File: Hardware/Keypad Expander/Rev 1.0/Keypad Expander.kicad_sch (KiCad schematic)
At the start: 11 parts, among them J1 6502 Card Edge, J2 PORT B, J3 PORT A, U1 65C21, U2 AT28C64, U3 74HC138, U4 74HC138

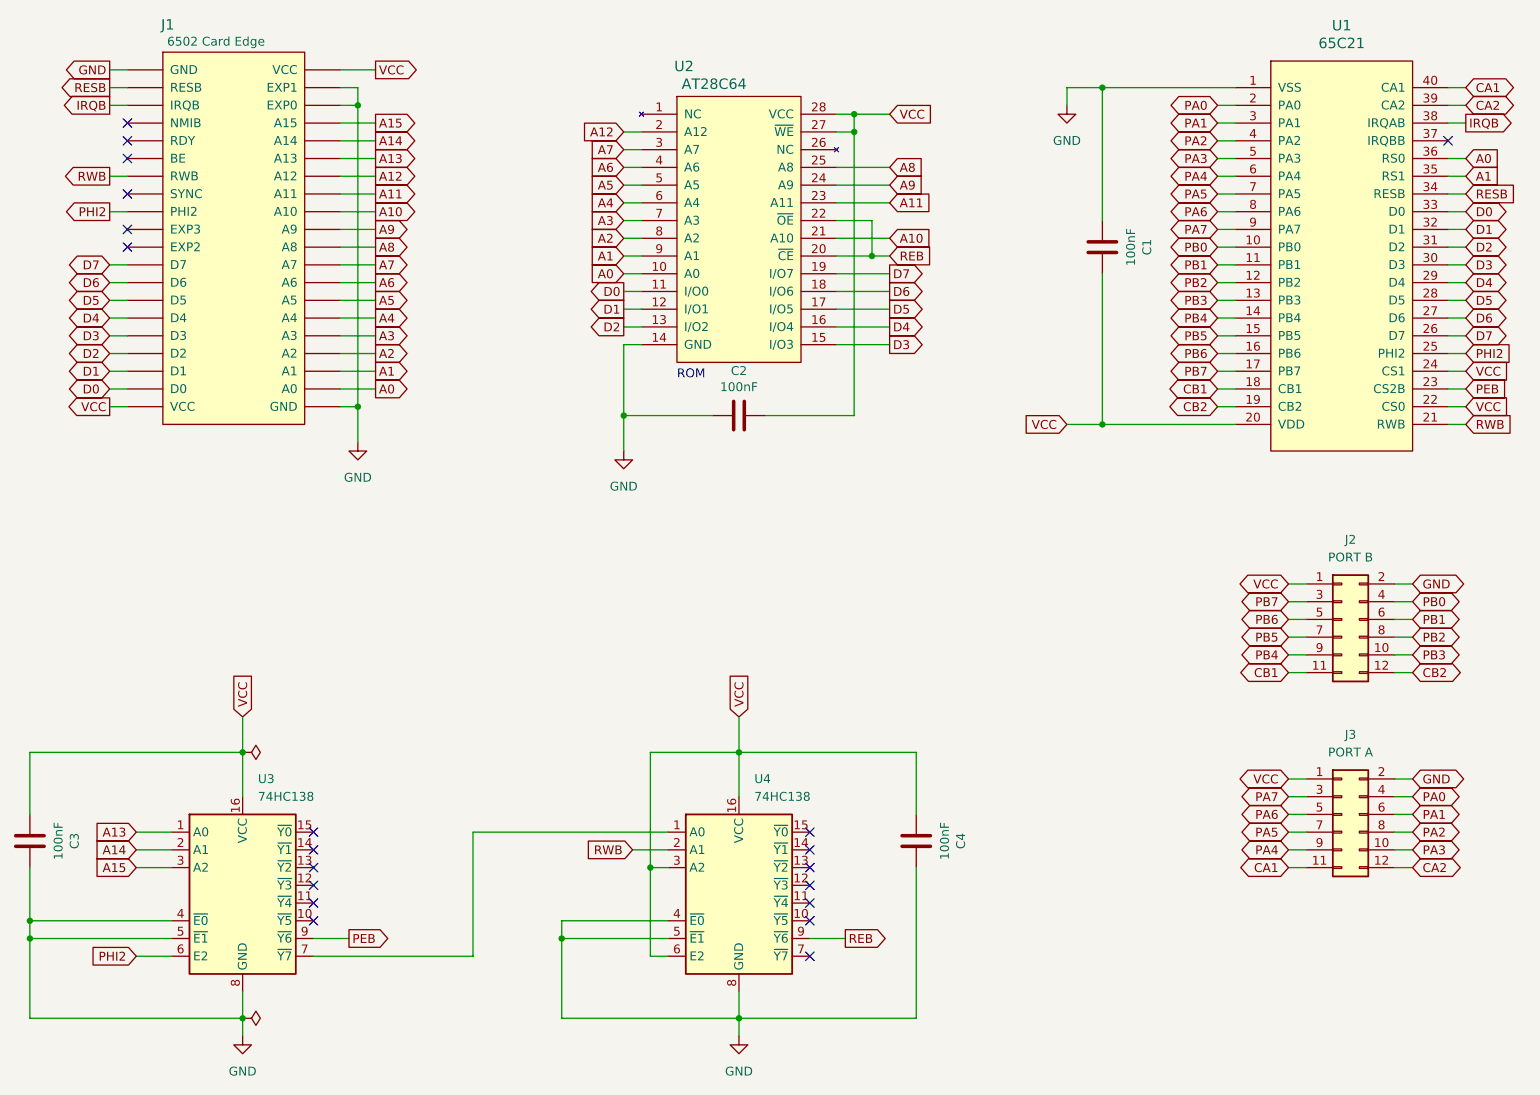
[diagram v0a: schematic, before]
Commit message: Finish Keypad Expander layout
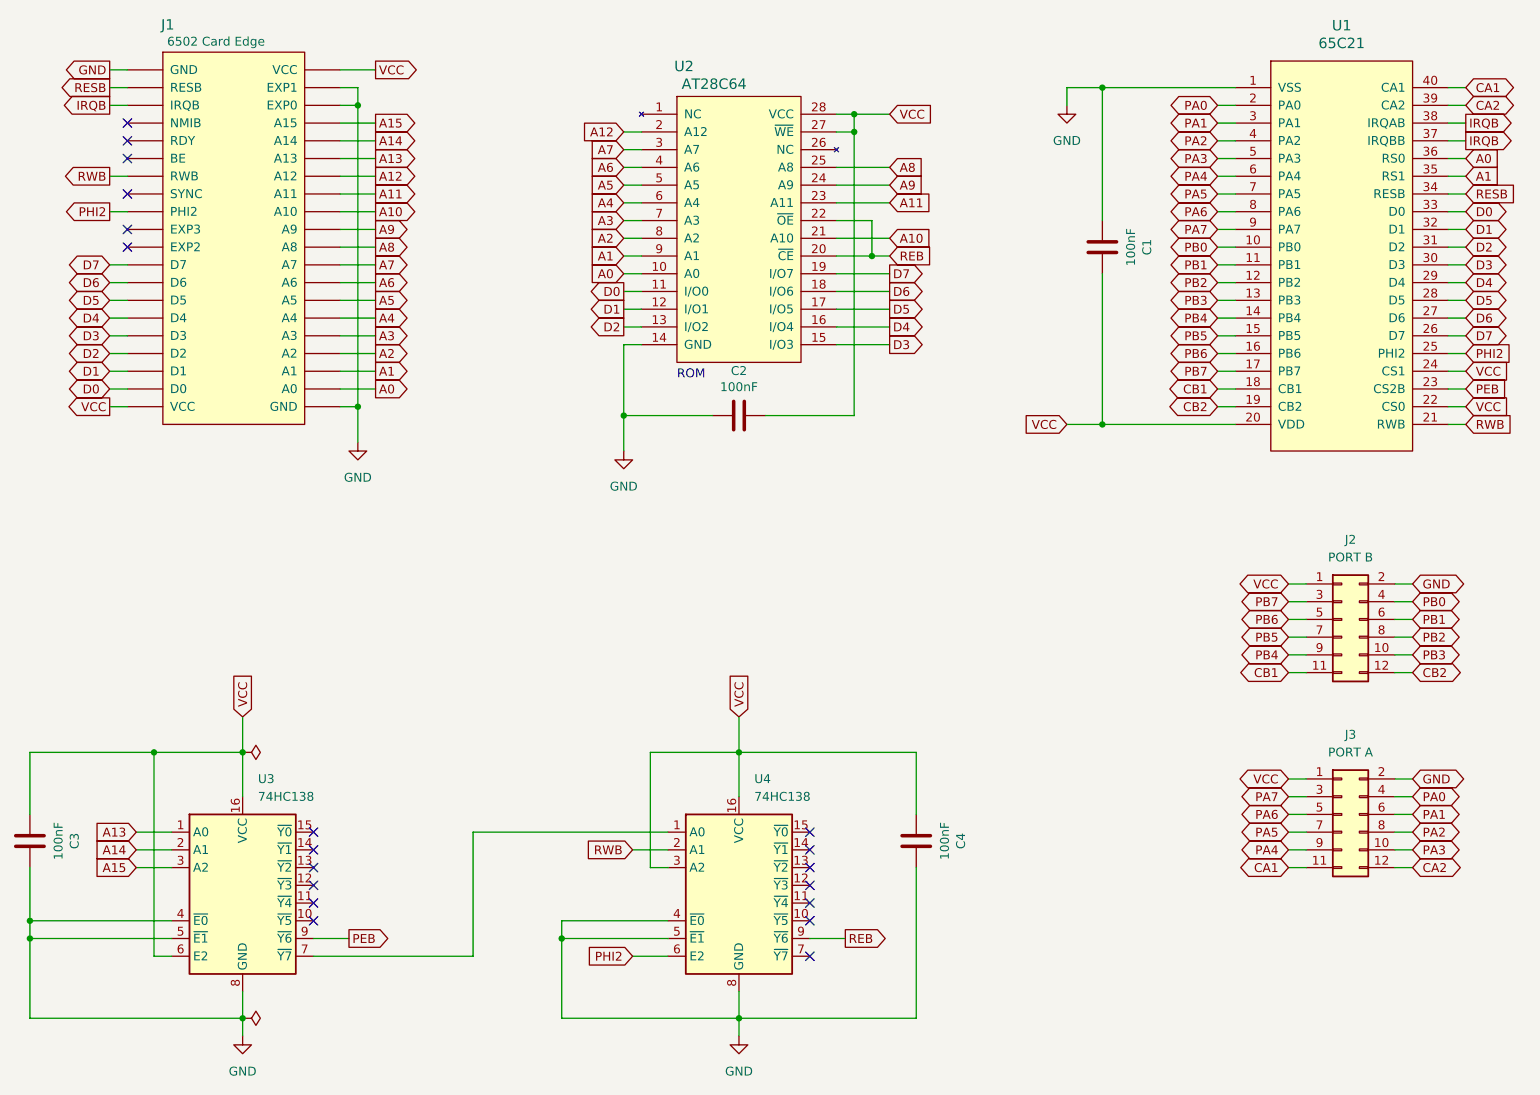
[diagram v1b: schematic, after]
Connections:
- net IRQB: now also U1.37 (IRQBB)
- net PHI2: now also U4.6 (E2); no longer U3.6 (E2)
- net VCC: now also U3.6 (E2); no longer U4.6 (E2)
- no-connect marks 20 -> 19
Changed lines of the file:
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@@
 	)
 	(junction
-		(at 114.3 153.67)
-		(diameter 0)
-		(color 0 0 0 0)
-	)
-	(junction
 		(at 179.07 41.91)
 		(diameter 0)
@@
 	)
 	(junction
+		(at 43.18 137.16)
+		(diameter 0)
+		(color 0 0 0 0)
+	)
+	(junction
 		(at 143.51 45.72)
 		(diameter 0)
@@
 	)
 	(no_connect
-		(at 228.6 49.53)
-	)
-	(no_connect
 		(at 66.04 148.59)
 	)
@@
 	(wire
 		(pts
+			(xy 45.72 166.37) (xy 43.18 166.37)
+		)
+		(stroke
+			(width 0)
+			(type default)
+		)
+	)
+	(wire
+		(pts
 			(xy 195.58 77.47) (xy 198.12 77.47)
 		)
@@
 	(wire
 		(pts
+			(xy 43.18 166.37) (xy 43.18 137.16)
+		)
+		(stroke
+			(width 0)
+			(type default)
+		)
+	)
+	(wire
+		(pts
 			(xy 205.74 123.19) (xy 208.28 123.19)
 		)
@@
 	(wire
 		(pts
-			(xy 55.88 137.16) (xy 25.4 137.16)
+			(xy 55.88 137.16) (xy 43.18 137.16)
 		)
 		(stroke
@@
 	(wire
 		(pts
-			(xy 116.84 166.37) (xy 114.3 166.37)
-		)
-		(stroke
-			(width 0)
-			(type default)
-		)
-	)
-	(wire
-		(pts
 			(xy 36.83 77.47) (xy 39.37 77.47)
 		)
@@
 	(wire
 		(pts
-			(xy 40.64 166.37) (xy 45.72 166.37)
+			(xy 140.97 45.72) (xy 143.51 45.72)
 		)
 		(stroke
@@
 	(wire
 		(pts
-			(xy 140.97 45.72) (xy 143.51 45.72)
+			(xy 69.85 80.01) (xy 74.93 80.01)
 		)
 		(stroke
@@
 	(wire
 		(pts
-			(xy 69.85 80.01) (xy 74.93 80.01)
+			(xy 43.18 137.16) (xy 25.4 137.16)
 		)
 		(stroke
@@
 	(wire
 		(pts
-			(xy 114.3 166.37) (xy 114.3 153.67)
-		)
-		(stroke
-			(width 0)
-			(type default)
-		)
-	)
-	(wire
-		(pts
 			(xy 148.59 68.58) (xy 140.97 68.58)
 		)
@@
 	(wire
 		(pts
+			(xy 111.76 166.37) (xy 116.84 166.37)
+		)
+		(stroke
+			(width 0)
+			(type default)
+		)
+	)
+	(wire
+		(pts
+			(xy 228.6 49.53) (xy 231.14 49.53)
+		)
+		(stroke
+			(width 0)
+			(type default)
+		)
+	)
+	(wire
+		(pts
 			(xy 152.4 137.16) (xy 127 137.16)
 		)
@@
 		)
 	)
-	(global_label "PHI2"
-		(shape input)
-		(at 40.64 166.37 180)
-		(effects
-			(font
-				(size 1.27 1.27)
-			)
-			(justify right)
-		)
-		(property "Intersheetrefs" "${INTERSHEET_REFS}"
-			(at 40.64 166.37 0)
-			(hide yes)
-			(show_name no)
-			(do_not_autoplace no)
-			(effects
-				(font
-					(size 1.27 1.27)
-				)
-			)
-		)
-	)
 	(global_label "A10"
 		(shape output)
@@
 		)
 	)
+	(global_label "PHI2"
+		(shape input)
+		(at 111.76 166.37 180)
+		(effects
+			(font
+				(size 1.27 1.27)
+			)
+			(justify right)
+		)
+		(property "Intersheetrefs" "${INTERSHEET_REFS}"
+			(at 111.76 166.37 0)
+			(hide yes)
+			(show_name no)
+			(do_not_autoplace no)
+			(effects
+				(font
+					(size 1.27 1.27)
+				)
+			)
+		)
+	)
 	(global_label "A14"
 		(shape input)
@@
 			)
 		)
+	)
+	(global_label "IRQB"
+		(shape output)
+		(at 231.14 49.53 0)
+		(effects
+			(font
+				(size 1.27 1.27)
+			)
+			(justify left)
+		)
+		(property "Intersheetrefs" "${INTERSHEET_REFS}"
+			(at 231.14 49.53 0)
+			(hide yes)
+			(show_name no)
+			(do_not_autoplace no)
+			(effects
+				(font
+					(size 1.27 1.27)
+				)
+			)
+		)
